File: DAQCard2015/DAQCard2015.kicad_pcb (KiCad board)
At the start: 4 copper layers, 160 x 160 mm, 211 parts, among them CON1 BARREL_JACK, K1 1462042-8, P1 QTH-090-01-F-D-A, P10 SPYPAD, P11 70246-1004, P2 QTH-090-01-F-D-A, P3 miniDIL20, P4 LEMO_EPY.00.250.NTN, P5 LEMO_EPY.00.250.NTN, P6 FAN, P7 CONN_02X20_Double, P8 SPYPAD, P9 SHV, Q1 MMBT2222A-TP, Q2 SBC817-40LT1G, SW1 DPDT, U1 RJ45x8, U10 AD9219, U11 THS4524IDBTR, U12 AD9219, U13 THS4524IDBTR, U14 AD9219, U15 THS4524IDBTR, U16 AD9219, U17 THS4524IDBTR, U18 AD9219, U19 AD8534, U2 AD5628, U20 LM1086_1V8, U21 LT1913, U22 AD5628, U23 AD8534, U24 MCP65R41, U25 LM1086_2V5, U3 THS4524IDBTR, U4 AD9219, U5 THS4524IDBTR, U6 AD9219, U7 THS4524IDBTR, U8 AD9219, U9 THS4524IDBTR

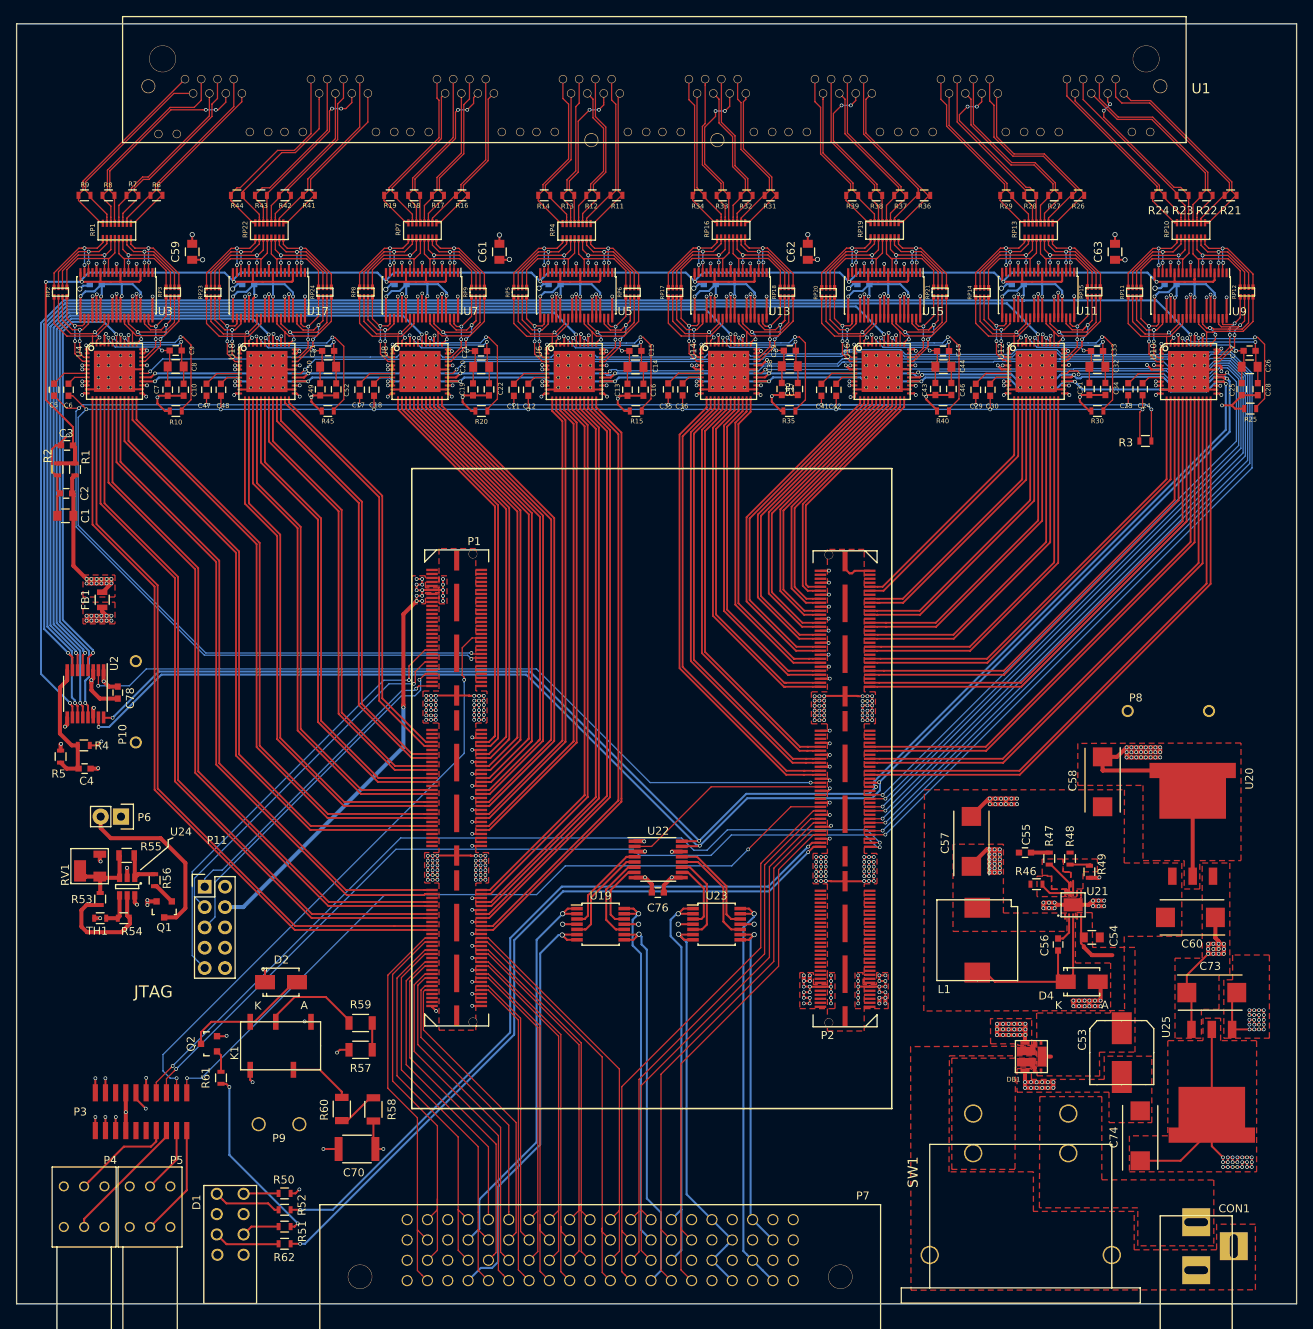
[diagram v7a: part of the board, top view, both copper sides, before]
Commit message: Update V1.0 of DAQ Board Includes LED Driver for RJ45 Port, repositioning of JTAG
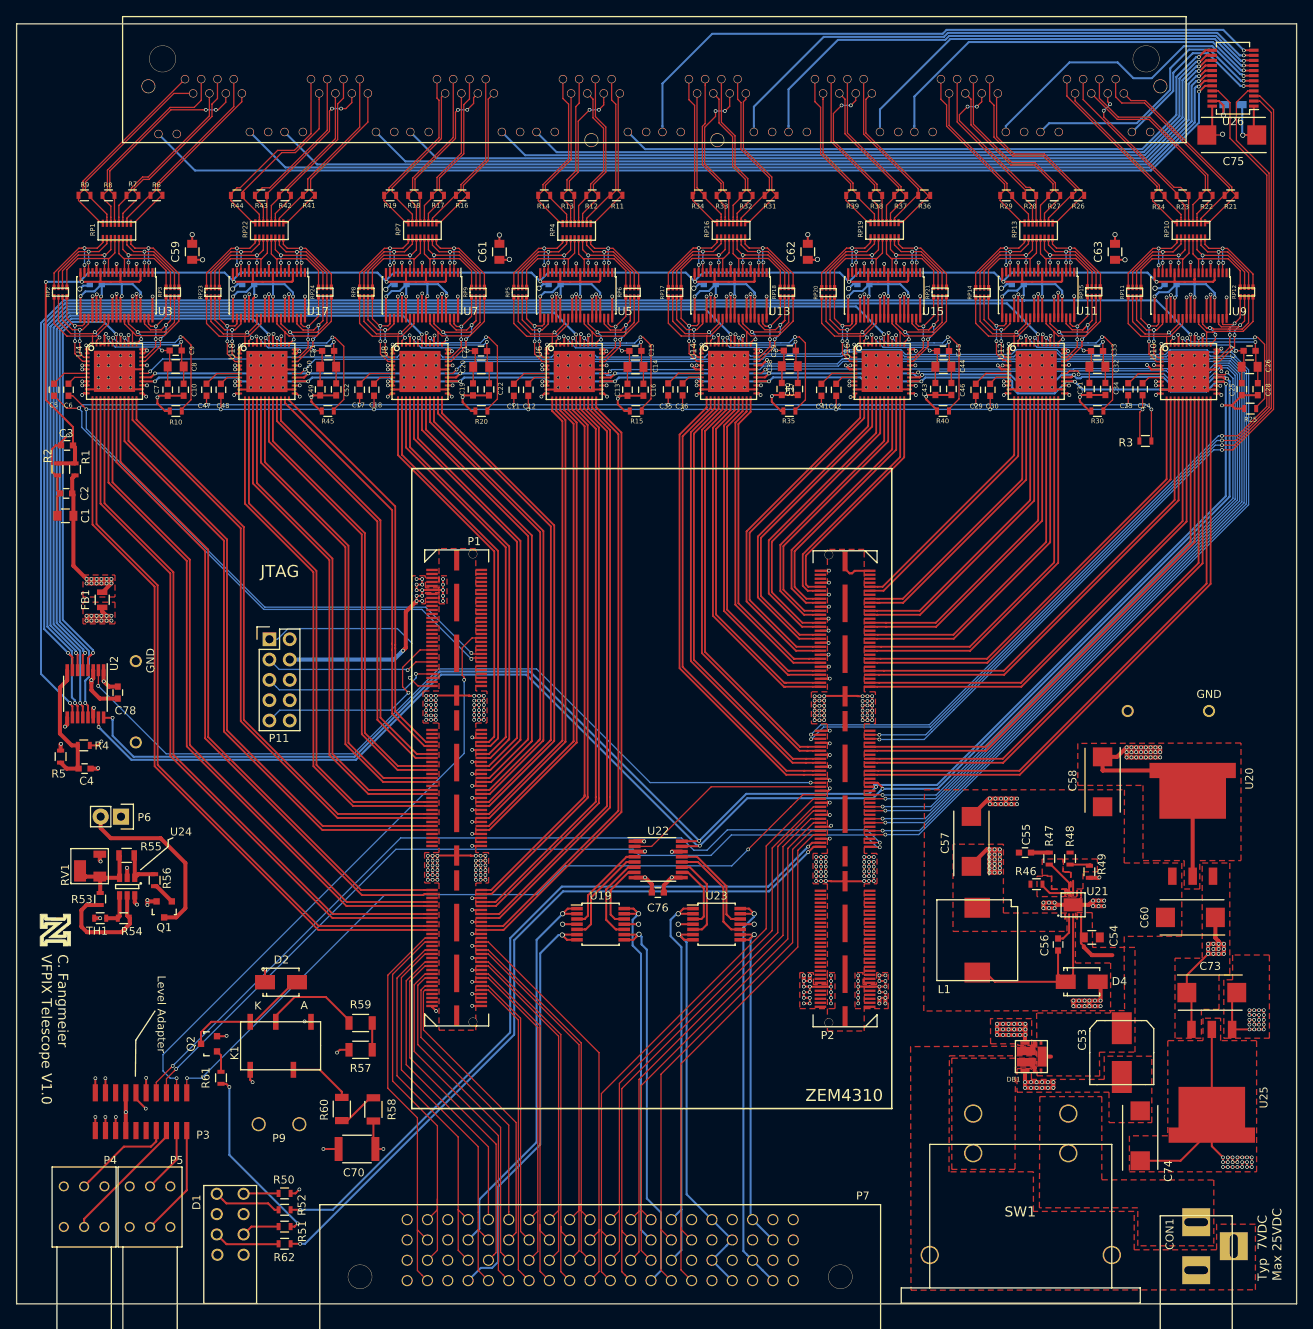
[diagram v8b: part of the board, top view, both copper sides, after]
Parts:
- added C75: 47uF, Capacitors_Tantalum_SMD:TantalC_SizeD_EIA-7343_Reflow, F.Cu at (169.9, 38.1)
- added G***: LOGO, extras:NLOGO, F.Cu at (22.9, 137.5)
- added R63: R, Resistors_SMD:R_0603_HandSoldering, B.Cu at (170.1, 34.3)
- added U26: TLC59282, Housings_SSOP:SSOP-24_3.9x8.7mm_Pitch0.635mm, F.Cu at (170.1, 31.0)
- P10, P8: value SPYPAD -> GND
- moved P11 32.0 mm to (49.6, 101.1)
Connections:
- P1 pad 145: IS1 -> (no net)
- P1 pad 147: Reset -> NULL
- P2 pad 115: (no net) -> RJ45_LED_LATCH
- P2 pad 116: (no net) -> RJ45_LED_CLK
- P2 pad 117: (no net) -> RJ45_LED_BLANK
- P2 pad 118: (no net) -> RJ45_LED_SDA
- P2 pad 81: EXT_TRG -> IS1
- P2 pad 85: (no net) -> Reset
- P2 pad 87: (no net) -> EXT_TRG
- U1 pad 10: (no net) -> 3V3dig
- U1 pad 11: (no net) -> RJ45_LED_14
- U1 pad 12: (no net) -> 3V3dig
- U1 pad 21: (no net) -> RJ45_LED_13
- U1 pad 22: (no net) -> 3V3dig
- U1 pad 23: (no net) -> RJ45_LED_12
- U1 pad 24: (no net) -> 3V3dig
- U1 pad 33: (no net) -> RJ45_LED_11
- U1 pad 34: (no net) -> 3V3dig
- U1 pad 35: (no net) -> RJ45_LED_10
- U1 pad 36: (no net) -> 3V3dig
- U1 pad 45: (no net) -> RJ45_LED_09
- U1 pad 46: (no net) -> 3V3dig
- U1 pad 47: (no net) -> RJ45_LED_08
- U1 pad 48: (no net) -> 3V3dig
- U1 pad 57: (no net) -> RJ45_LED_07
- U1 pad 58: (no net) -> 3V3dig
- U1 pad 59: (no net) -> RJ45_LED_06
- U1 pad 60: (no net) -> 3V3dig
- U1 pad 69: (no net) -> RJ45_LED_05
- U1 pad 70: (no net) -> 3V3dig
- U1 pad 71: (no net) -> RJ45_LED_04
- U1 pad 72: (no net) -> 3V3dig
- U1 pad 81: (no net) -> RJ45_LED_03
- U1 pad 82: (no net) -> 3V3dig
- U1 pad 83: (no net) -> RJ45_LED_02
- U1 pad 84: (no net) -> 3V3dig
- U1 pad 9: (no net) -> RJ45_LED_15
- U1 pad 93: (no net) -> RJ45_LED_01
- U1 pad 94: (no net) -> 3V3dig
- U1 pad 95: (no net) -> RJ45_LED_00
- U1 pad 96: (no net) -> 3V3dig
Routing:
- net RJ45_LED_15: track 0.00 -> 140.3 mm, vias 0 -> 1
- net RJ45_LED_14: track 0.00 -> 129.1 mm, vias 0 -> 1
- net RJ45_LED_13: track 0.00 -> 124.8 mm, vias 0 -> 1
- net RJ45_LED_LATCH: track 0.00 -> 118.2 mm, vias 0 -> 2
- net RJ45_LED_BLANK: track 0.00 -> 117.9 mm, vias 0 -> 2
- net RJ45_LED_12: track 0.00 -> 113.4 mm, vias 0 -> 1
- net RJ45_LED_11: track 0.00 -> 109.1 mm, vias 0 -> 1
- net RJ45_LED_CLK: track 0.00 -> 108.2 mm, vias 0 -> 2
- net RJ45_LED_SDA: track 0.00 -> 106.9 mm, vias 0 -> 2
- net RJ45_LED_10: track 0.00 -> 97.7 mm, vias 0 -> 1
- net RJ45_LED_09: track 0.00 -> 93.3 mm, vias 0 -> 1
- net RJ45_LED_07: track 0.00 -> 83.8 mm, vias 0 -> 1
- net RJ45_LED_08: track 0.00 -> 81.9 mm, vias 0 -> 1
- net RJ45_LED_06: track 0.00 -> 70.6 mm, vias 0 -> 1
- net RJ45_LED_05: track 0.00 -> 67.6 mm, vias 0 -> 1
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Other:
- board text added: "C. Fangmeier VFPIX Telescope V1.0"
- board text added: "Level Adapter"
- board text added: "Typ 7VDC Max 25VDC"
- board text added: "ZEM4310"
